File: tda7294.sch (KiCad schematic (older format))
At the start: 58 parts, among them J1 Screw_Terminal_01x04, J2 Screw_Terminal_01x04, J3 Screw_Terminal_01x02, J4 Screw_Terminal_01x03, Q1 BSS84, Q2 2N7002, U1 TDA7293, U2 TDA7293, U3 PC817, U4 MCP1792

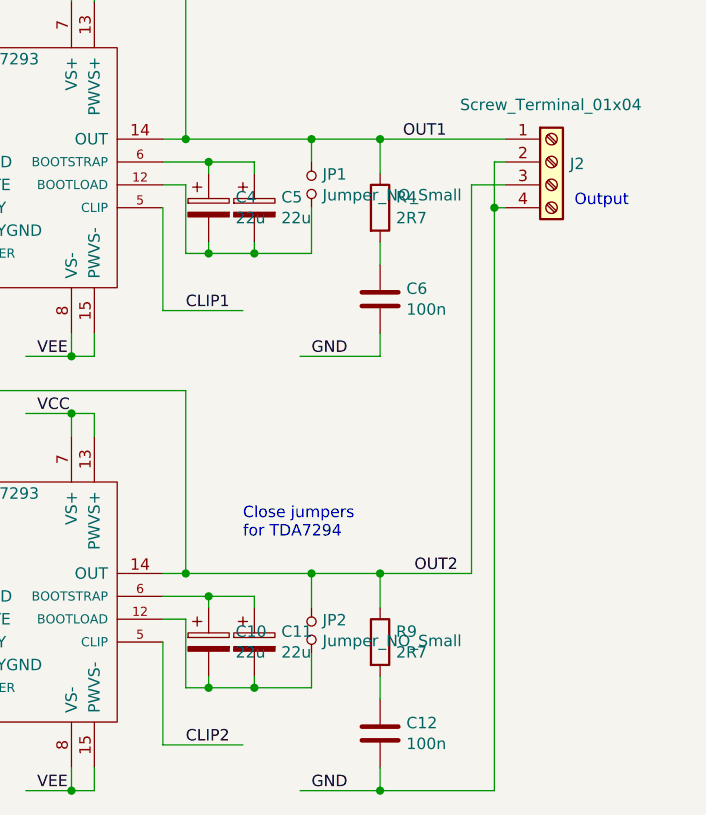
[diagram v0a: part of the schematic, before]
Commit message: Re-routed to separate the signal, power and output grounds
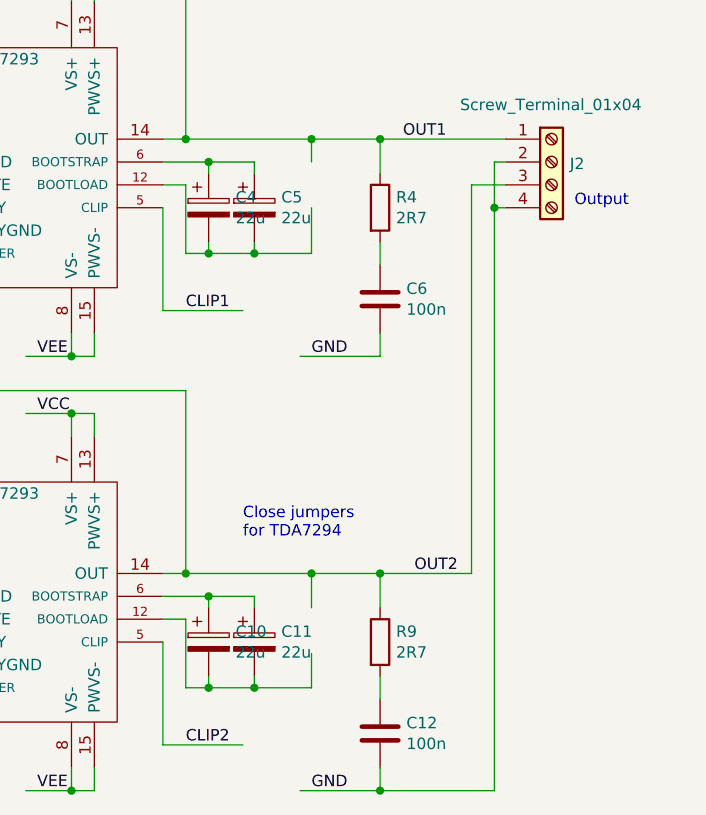
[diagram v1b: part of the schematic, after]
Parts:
- removed JP1, JP2: Jumper_NO_Small, Pin_Headers:Pin_Header_Straight_1x02_Pitch2.00mm, symbol Device:Jumper_NO_Small
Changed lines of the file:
@@
 Text Notes 5850 1450 0    50   ~ 0
 Alt Footprints\nfor 22u/50V\nelectrolytics
-$Comp
-L Device:Jumper_NO_Small JP1
-U 1 1 61EC7F7C
-P 9200 2300
-F 0 "JP1" V 9154 2348 50  0000 L CNN
-F 1 "Jumper_NO_Small" V 9245 2348 50  0000 L CNN
-F 2 "Pin_Headers:Pin_Header_Straight_1x02_Pitch2.00mm" H 9200 2300 50  0001 C CNN
-F 3 "~" H 9200 2300 50  0001 C CNN
-	1    9200 2300
-	0    1    1    0
-$EndComp
 Wire Wire Line
 	9200 2100 9200 2200
@@
 	9200 2600 8950 2600
 Connection ~ 8950 2600
-$Comp
-L Device:Jumper_NO_Small JP2
-U 1 1 61EEC3A9
-P 9200 4250
-F 0 "JP2" V 9154 4298 50  0000 L CNN
-F 1 "Jumper_NO_Small" V 9245 4298 50  0000 L CNN
-F 2 "Pin_Headers:Pin_Header_Straight_1x02_Pitch2.00mm" H 9200 4250 50  0001 C CNN
-F 3 "~" H 9200 4250 50  0001 C CNN
-	1    9200 4250
-	0    1    1    0
-$EndComp
 Wire Wire Line
 	9200 4150 9200 4000
